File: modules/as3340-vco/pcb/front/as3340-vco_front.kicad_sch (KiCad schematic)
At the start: 41 parts

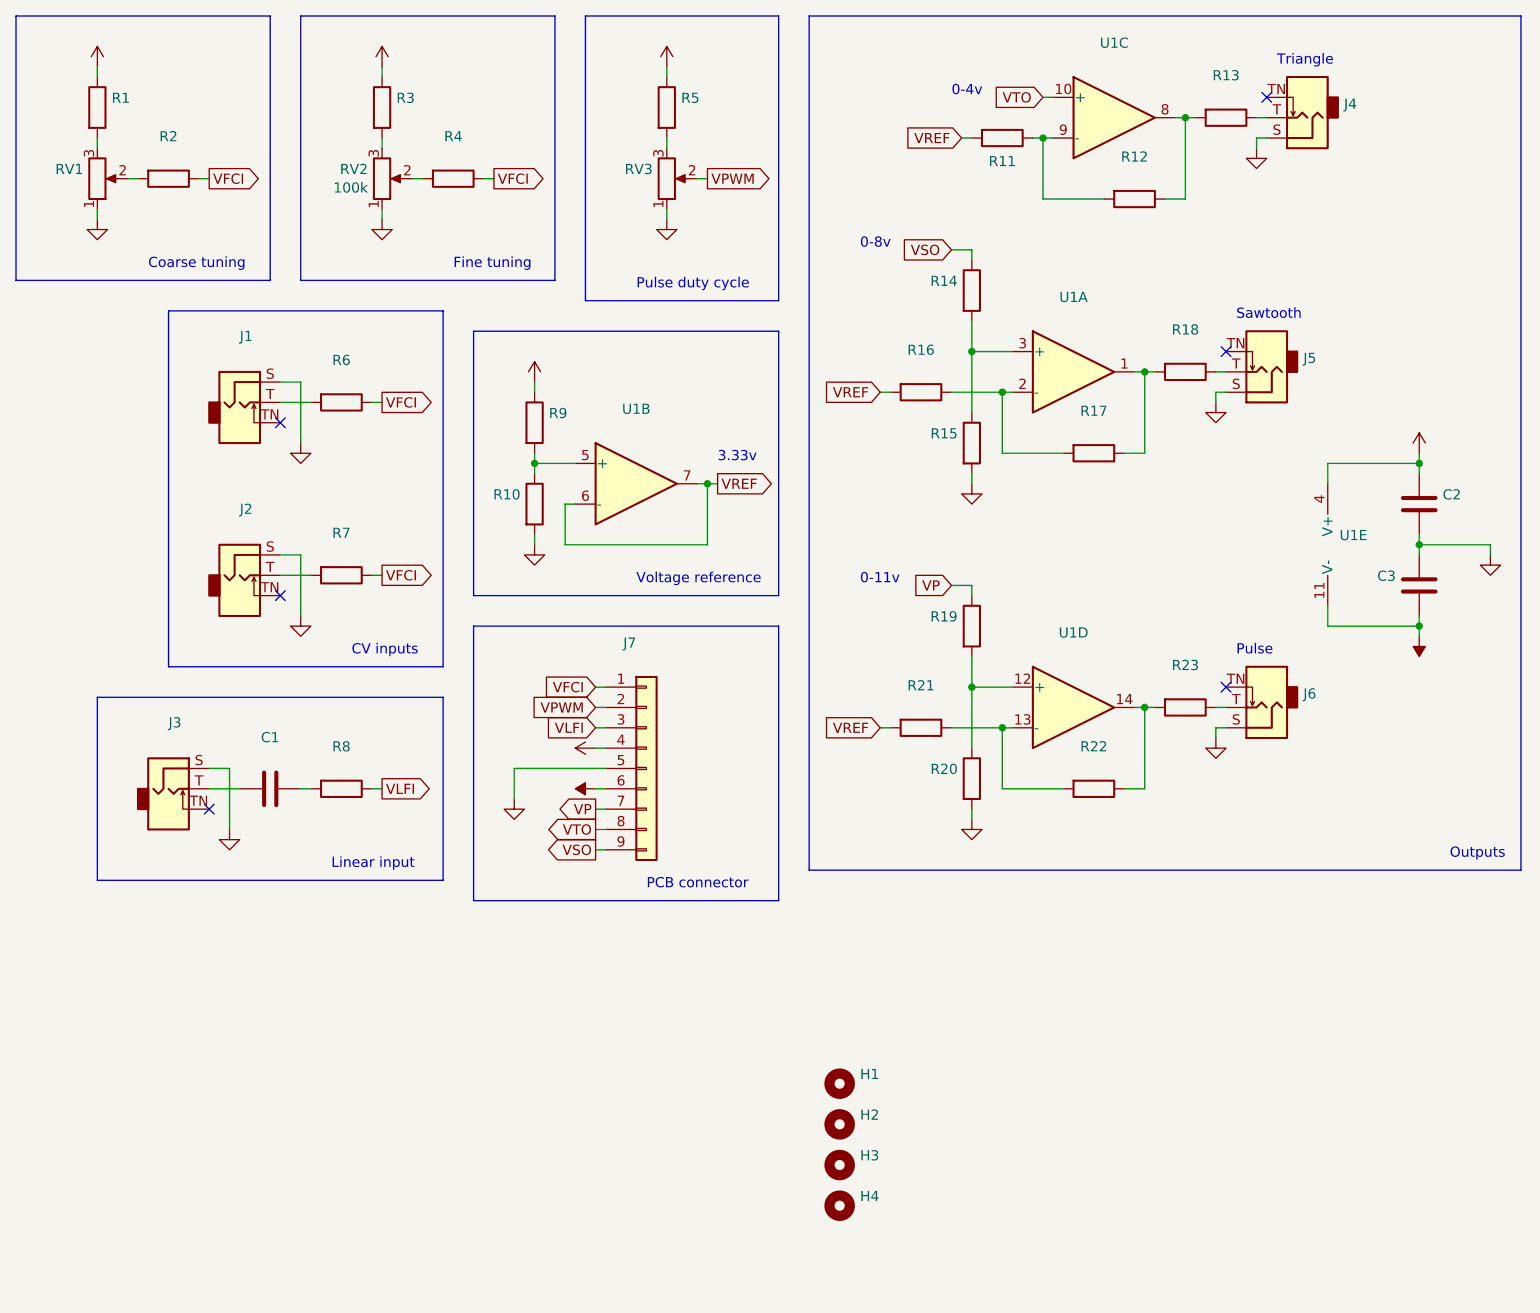
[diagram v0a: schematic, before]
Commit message: modules: as3340-vco: front: revision A (redesign)
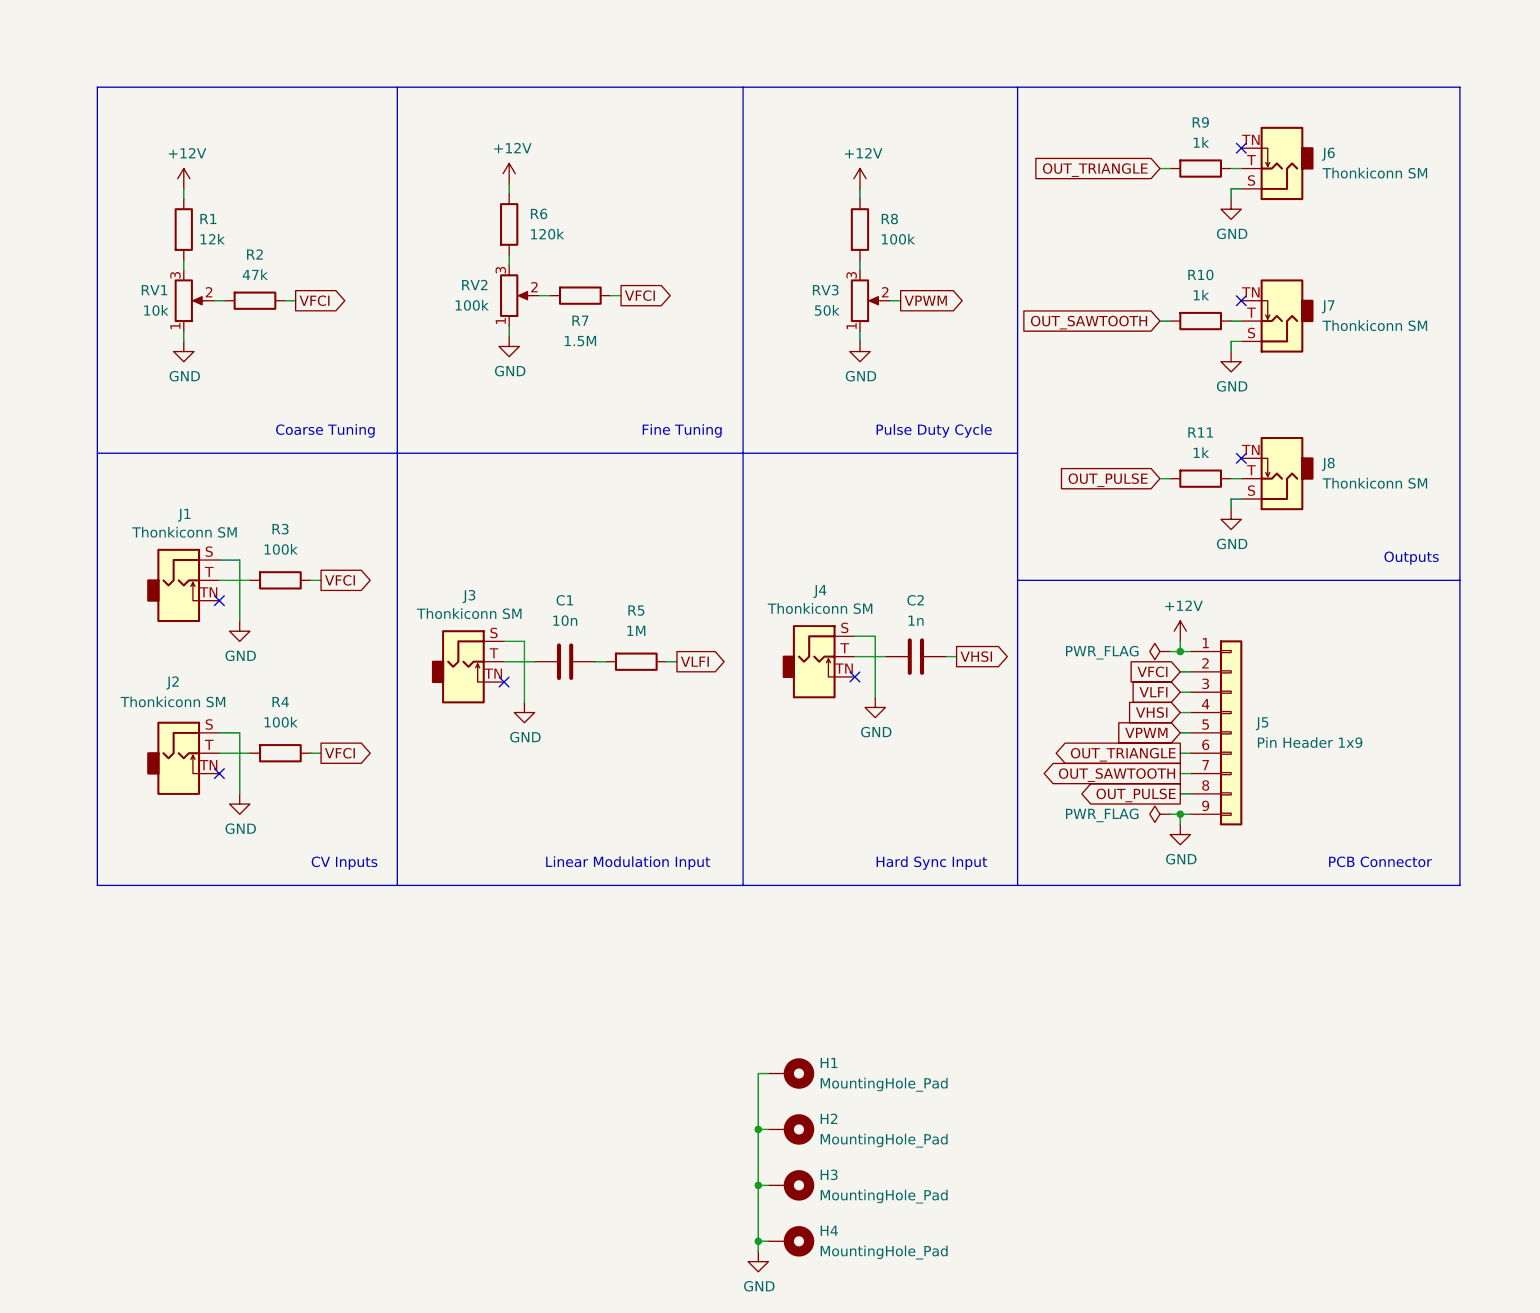
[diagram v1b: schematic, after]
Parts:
- removed C3: (no value), symbol Device:C
- removed H1, H2, H3, H4: (no value), symbol Mechanical:MountingHole
- removed J5: (no value), symbol Connector:AudioJack2_SwitchT
- removed J7: (no value), symbol Connector_Generic:Conn_01x09
- removed R12, R13, R14, R15, R16, R17, R18, R19, R20, R21, R22, R23: (no value), symbol Device:R
- removed U1: (no value), symbol Amplifier_Operational:TL074
- added H1, H2, H3, H4: MountingHole_Pad, MountingHole:MountingHole_2.2mm_M2_Pad_Via, symbol Mechanical:MountingHole_Pad
- added J5: Pin Header 1x9, Connector_PinHeader_2.54mm:PinHeader_1x09_P2.54mm_Vertical, symbol Connector_Generic:Conn_01x09
- added J7, J8: Thonkiconn SM, eurorack:Jack_3.5mm_QingPu_WQP-PJ398SM_Vertical, symbol Connector:AudioJack2_SwitchT
- C1: value (none) -> 10n; footprint (none) -> Capacitor_THT:C_Disc_D3.0mm_W1.6mm_P2.50mm
- C2: value (none) -> 1n; footprint (none) -> Capacitor_THT:C_Disc_D3.0mm_W1.6mm_P2.50mm
- J1, J2, J3, J4, J6: value (none) -> Thonkiconn SM; footprint (none) -> eurorack:Jack_3.5mm_QingPu_WQP-PJ398SM_Vertical
- R1: value (none) -> 12k; footprint (none) -> Resistor_THT:R_Axial_DIN0207_L6.3mm_D2.5mm_P10.16mm_Horizontal
- R10, R11, R9: value (none) -> 1k; footprint (none) -> Resistor_THT:R_Axial_DIN0207_L6.3mm_D2.5mm_P10.16mm_Horizontal
- R2: value (none) -> 47k; footprint (none) -> Resistor_THT:R_Axial_DIN0207_L6.3mm_D2.5mm_P10.16mm_Horizontal
- R3: renamed from R6; value (none) -> 100k; footprint (none) -> Resistor_THT:R_Axial_DIN0207_L6.3mm_D2.5mm_P10.16mm_Horizontal
- R4: renamed from R7; value (none) -> 100k; footprint (none) -> Resistor_THT:R_Axial_DIN0207_L6.3mm_D2.5mm_P10.16mm_Horizontal
- R5: renamed from R8; value (none) -> 1M; footprint (none) -> Resistor_THT:R_Axial_DIN0207_L6.3mm_D2.5mm_P10.16mm_Horizontal
- R6: renamed from R3; value (none) -> 120k; footprint (none) -> Resistor_THT:R_Axial_DIN0207_L6.3mm_D2.5mm_P10.16mm_Horizontal
- R7: renamed from R4; value (none) -> 1.5M; footprint (none) -> Resistor_THT:R_Axial_DIN0207_L6.3mm_D2.5mm_P10.16mm_Horizontal
- R8: renamed from R5; value (none) -> 100k; footprint (none) -> Resistor_THT:R_Axial_DIN0207_L6.3mm_D2.5mm_P10.16mm_Horizontal
- RV1: value (none) -> 10k; footprint (none) -> Potentiometer_THT:Potentiometer_Alpha_RD901F-40-00D_Single_Vertical_CircularHoles
- RV3: value (none) -> 50k; footprint (none) -> Potentiometer_THT:Potentiometer_Alpha_RD901F-40-00D_Single_Vertical_CircularHoles
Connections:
- net +12V: now also J5.1 (Pin_1); no longer C2.1, R9.1
- net GND: now also H1.1, H2.1, H3.1, H4.1, J5.9 (Pin_9), J7.S, J8.S; no longer C2.2, R10.2
- net VFCI: now also J5.2 (Pin_2)
- net VLFI: now also J5.3 (Pin_3)
- net VPWM: now also J5.5 (Pin_5)
- net at R10.1: now also J7.T; no longer R9.2
- net at J6.T: now also R9.1
- net at R11.1: now also J8.T
- net at J4.T: now also C2.2
- net VREF renamed OUT_PULSE
- net OUT_PULSE: now also J5.8 (Pin_8)
- new net OUT_SAWTOOTH: J5.7 (Pin_7), R10.2
- new net OUT_TRIANGLE: J5.6 (Pin_6), R9.2
- new net VHSI: C2.1, J5.4 (Pin_4)
- no-connect marks 6 -> 7
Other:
- note added: "CV Inputs"
- note added: "Coarse Tuning"
- note added: "Fine Tuning"
- note added: "Hard Sync Input"
- note added: "Linear Modulation Input"
- note added: "PCB Connector"
- note added: "Pulse Duty Cycle"
- note removed: "0-11v"
- note removed: "0-4v"
- note removed: "0-8v"
- note removed: "3.33v"
- note removed: "CV inputs"
- note removed: "Coarse tuning"
- note removed: "Fine tuning"
- note removed: "Linear input"
- note removed: "PCB connector"
- note removed: "Pulse"
- note removed: "Pulse duty cycle"
- note removed: "Sawtooth"
- note removed: "Triangle"
- note removed: "Voltage reference"
- company: (none) -> eurorack.rgm.io
- moved on the sheet: C1, J1, J2, J3, R1, R2, R3, R4, R5, R6, R7, R8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
